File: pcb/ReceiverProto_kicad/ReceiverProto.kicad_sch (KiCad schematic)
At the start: 0 parts

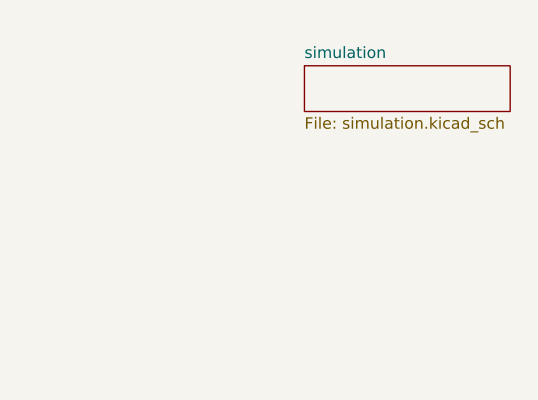
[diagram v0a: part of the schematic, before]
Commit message: more work on ADC driving interface, including negative power supply generation
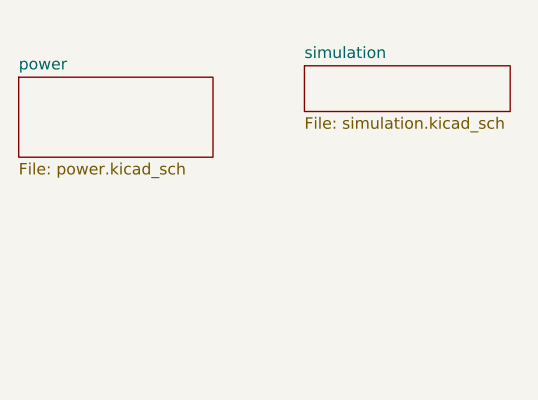
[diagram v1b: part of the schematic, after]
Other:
- added sheet power (power.kicad_sch)
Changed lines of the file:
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@@
+	)
+	(sheet
+		(at 71.12 97.79)
+		(size 21.59 8.89)
+		(exclude_from_sim no)
+		(in_bom yes)
+		(on_board yes)
+		(dnp no)
+		(fields_autoplaced yes)
+		(stroke
+			(width 0.1524)
+			(type solid)
+		)
+		(fill
+			(color 0 0 0 0.0000)
+		)
+		(property "Sheetname" "power"
+			(at 71.12 97.0784 0)
+			(effects
+				(font
+					(size 1.27 1.27)
+				)
+				(justify left bottom)
+			)
+		)
+		(property "Sheetfile" "power.kicad_sch"
+			(at 71.12 107.2646 0)
+			(effects
+				(font
+					(size 1.27 1.27)
+				)
+				(justify left top)
+			)
+		)
+		(instances
+			(project "ReceiverProto"
+				(path "/1f346c8c-1e51-4f75-85ee-2d30c45e3fc5"
+					(page "5")
+				)
+			)
+		)
 	)
 	(sheet

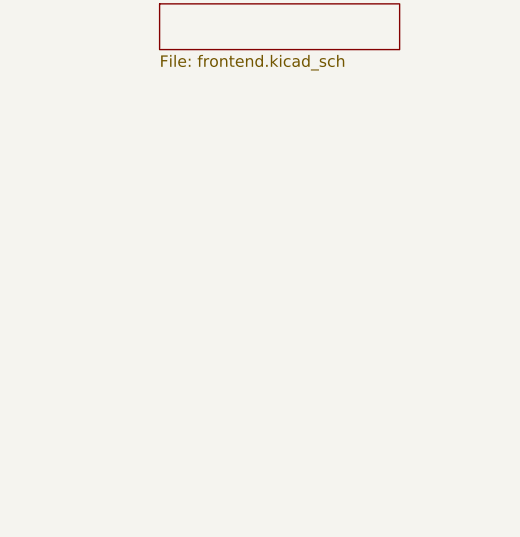
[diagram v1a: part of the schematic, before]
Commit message: added I/O for ADC interface, other slight tweaks
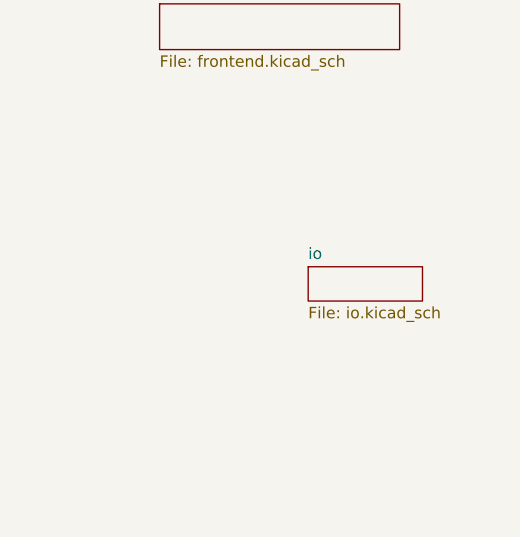
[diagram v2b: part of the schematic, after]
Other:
- added sheet io (io.kicad_sch)
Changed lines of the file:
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@@
+	)
+	(sheet
+		(at 176.53 123.19)
+		(size 12.7 3.81)
+		(exclude_from_sim no)
+		(in_bom yes)
+		(on_board yes)
+		(dnp no)
+		(fields_autoplaced yes)
+		(stroke
+			(width 0.1524)
+			(type solid)
+		)
+		(fill
+			(color 0 0 0 0.0000)
+		)
+		(property "Sheetname" "io"
+			(at 176.53 122.4784 0)
+			(effects
+				(font
+					(size 1.27 1.27)
+				)
+				(justify left bottom)
+			)
+		)
+		(property "Sheetfile" "io.kicad_sch"
+			(at 176.53 127.5846 0)
+			(effects
+				(font
+					(size 1.27 1.27)
+				)
+				(justify left top)
+			)
+		)
+		(instances
+			(project "ReceiverProto"
+				(path "/1f346c8c-1e51-4f75-85ee-2d30c45e3fc5"
+					(page "6")
+				)
+			)
+		)
 	)
 	(sheet
